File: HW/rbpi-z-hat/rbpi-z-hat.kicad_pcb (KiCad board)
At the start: 4 copper layers, 65 x 30 mm, 98 parts, among them IC1 BQ24315DSGR, J1 RBPI_CONN, J10 JST_GH, J11 Conn_01x10, J12 Conn_01x06, J13 Conn_01x10, J14 Conn_01x06, J15 Conn_01x06, J16 Conn_01x10, J8 Conn_01x06_MountingPin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

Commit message: Changes in Sch & PCB
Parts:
- removed RN9: 1K5, Resistor_SMD:R_Array_Concave_4x0402
- added R13: 1K5, Resistor_SMD:R_0402_1005Metric, F.Cu at (18.4, 19.7)
- added R14: 1K5, Resistor_SMD:R_0402_1005Metric, F.Cu at (18.4, 20.7)
- added R15: 1K5, Resistor_SMD:R_0402_1005Metric, F.Cu at (25.1, 21.1)
- added R16: 1K5, Resistor_SMD:R_0402_1005Metric, F.Cu at (25.1, 20.0)
- R1: footprint Resistor_SMD:R_0603_1608Metric -> Resistor_SMD:R_0402_1005Metric
- moved C5 17.5 mm to (28.1, 20.4), turned to 180 degrees
- moved R1 15.4 mm to (25.1, 18.9), turned to 0 degrees
- moved FB3 15.3 mm to (30.9, 19.4)
- moved U4 14.8 mm to (21.8, 20.1), turned to 0 degrees
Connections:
- net /BARO/BARO_MS_nCS renamed /MS_nCS

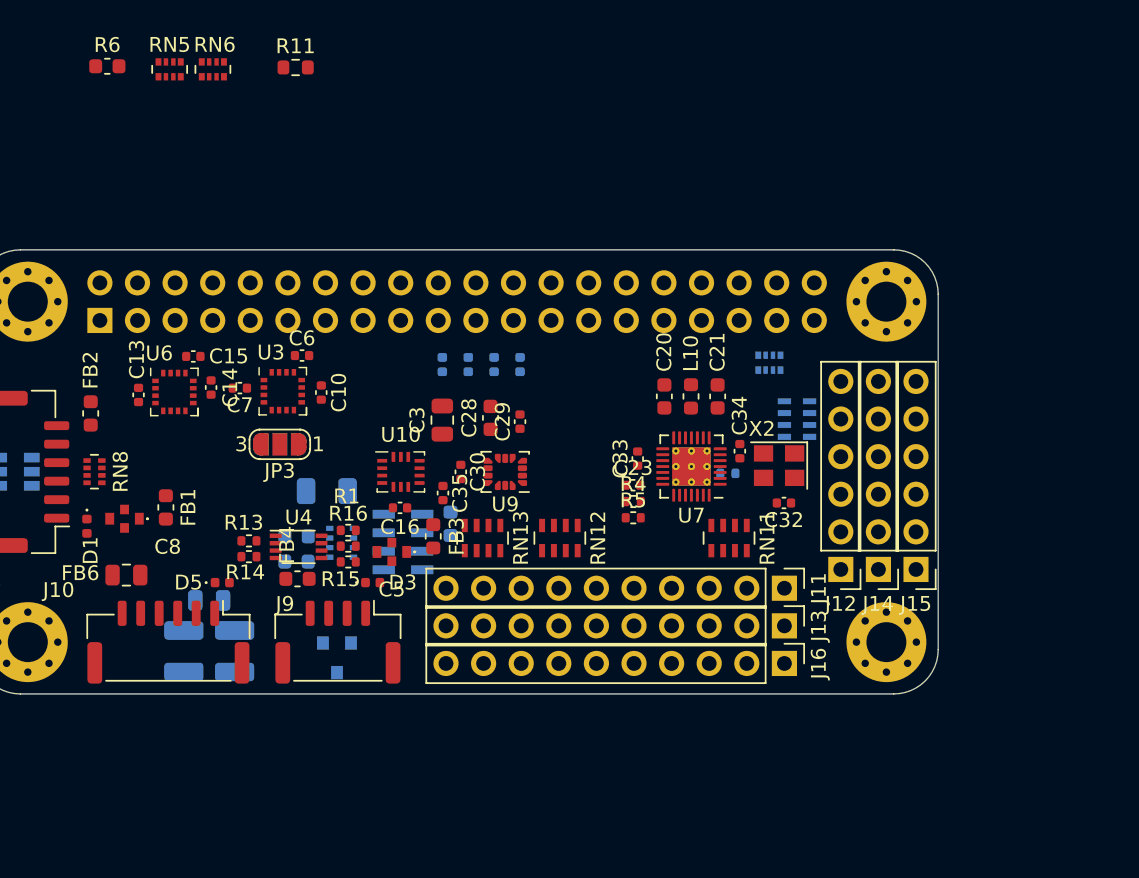
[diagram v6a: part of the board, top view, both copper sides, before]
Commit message: Changed some footprints
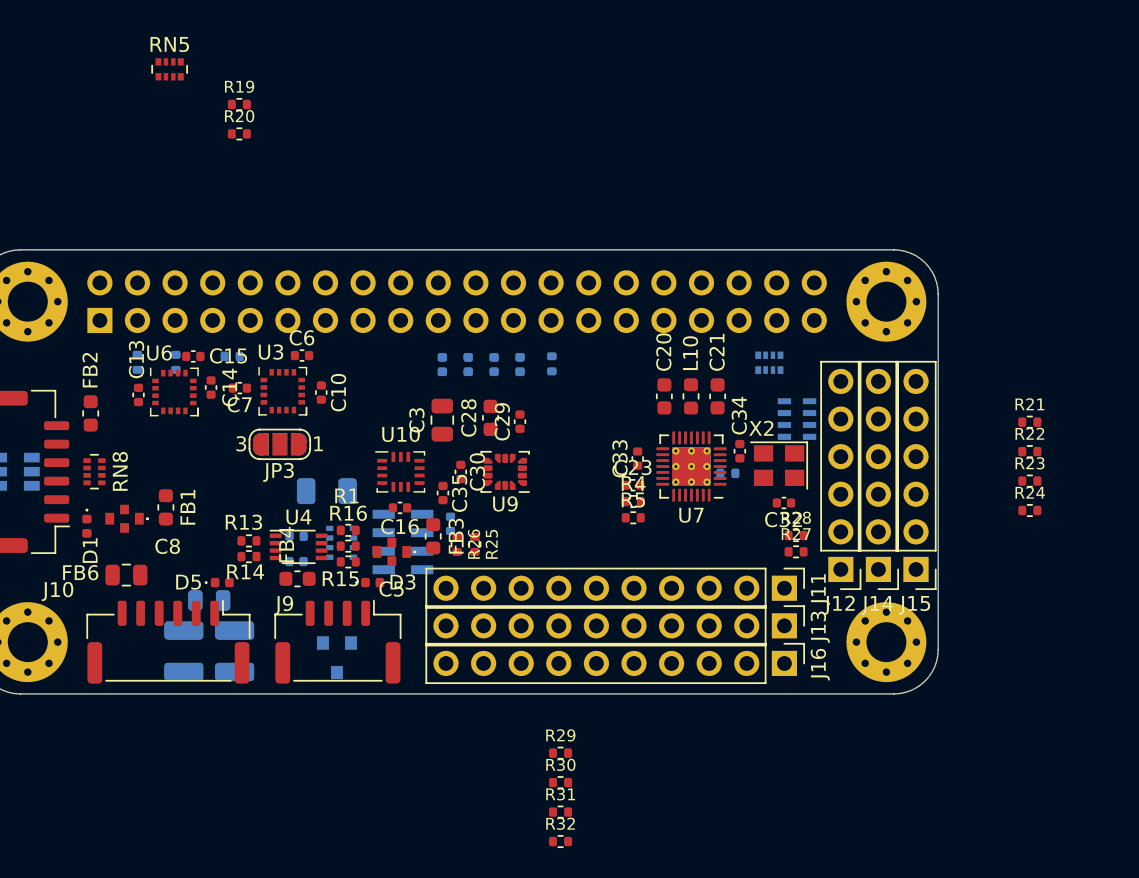
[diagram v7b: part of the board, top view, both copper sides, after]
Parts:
- removed RN11, RN12, RN13: 220R, Resistor_SMD:R_Array_Concave_4x0603
- removed RN6: 10K/4x0402, Resistor_SMD:R_Array_Convex_4x0402
- added R17: 10K, Resistor_SMD:R_0402_1005Metric, B.Cu at (10.9, 7.60)
- added R18: 10K, Resistor_SMD:R_0402_1005Metric, B.Cu at (13.5, 7.60)
- added R19: 10K, Resistor_SMD:R_0402_1005Metric, F.Cu at (17.8, -9.82)
- added R20: 10K, Resistor_SMD:R_0402_1005Metric, F.Cu at (17.8, -7.83)
- added R21: 220К, Resistor_SMD:R_0402_1005Metric, F.Cu at (71.2, 11.6)
- added R22: 220К, Resistor_SMD:R_0402_1005Metric, F.Cu at (71.2, 13.6)
- added R23: 220К, Resistor_SMD:R_0402_1005Metric, F.Cu at (71.2, 15.6)
- added R24: 220К, Resistor_SMD:R_0402_1005Metric, F.Cu at (71.2, 17.6)
- added R25: 220К, Resistor_SMD:R_0402_1005Metric, F.Cu at (33.7, 19.9)
- added R26: 220К, Resistor_SMD:R_0402_1005Metric, F.Cu at (32.5, 19.9)
- added R27: 220К, Resistor_SMD:R_0402_1005Metric, F.Cu at (55.4, 20.4)
- added R28: 220К, Resistor_SMD:R_0402_1005Metric, F.Cu at (55.4, 19.3)
- added R29: 220К, Resistor_SMD:R_0402_1005Metric, F.Cu at (39.5, 34.0)
- added R30: 220К, Resistor_SMD:R_0402_1005Metric, F.Cu at (39.5, 36.0)
- added R31: 220К, Resistor_SMD:R_0402_1005Metric, F.Cu at (39.5, 38.0)
- added R32: 220К, Resistor_SMD:R_0402_1005Metric, F.Cu at (39.5, 40.0)
- C2, C4, C9: footprint Capacitor_SMD:C_0603_1608Metric -> Capacitor_SMD:C_0402_1005Metric
- R11, R6: footprint Resistor_SMD:R_0603_1608Metric -> Resistor_SMD:R_0402_1005Metric; moved to B.Cu
- moved R11 26.5 mm to (38.9, 7.70), turned to 90 degrees
- moved R6 21.3 mm to (17.3, 7.20)

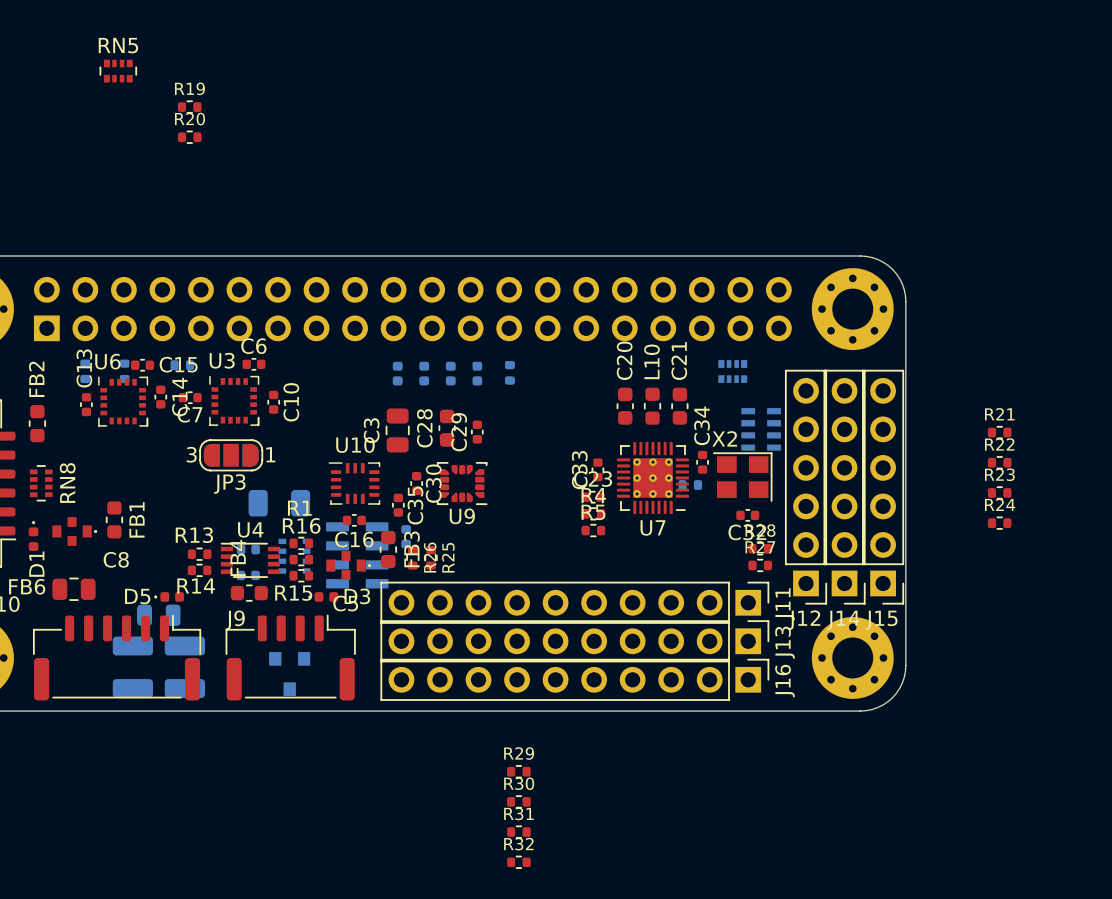
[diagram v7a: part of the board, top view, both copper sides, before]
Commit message: Changed some footprints
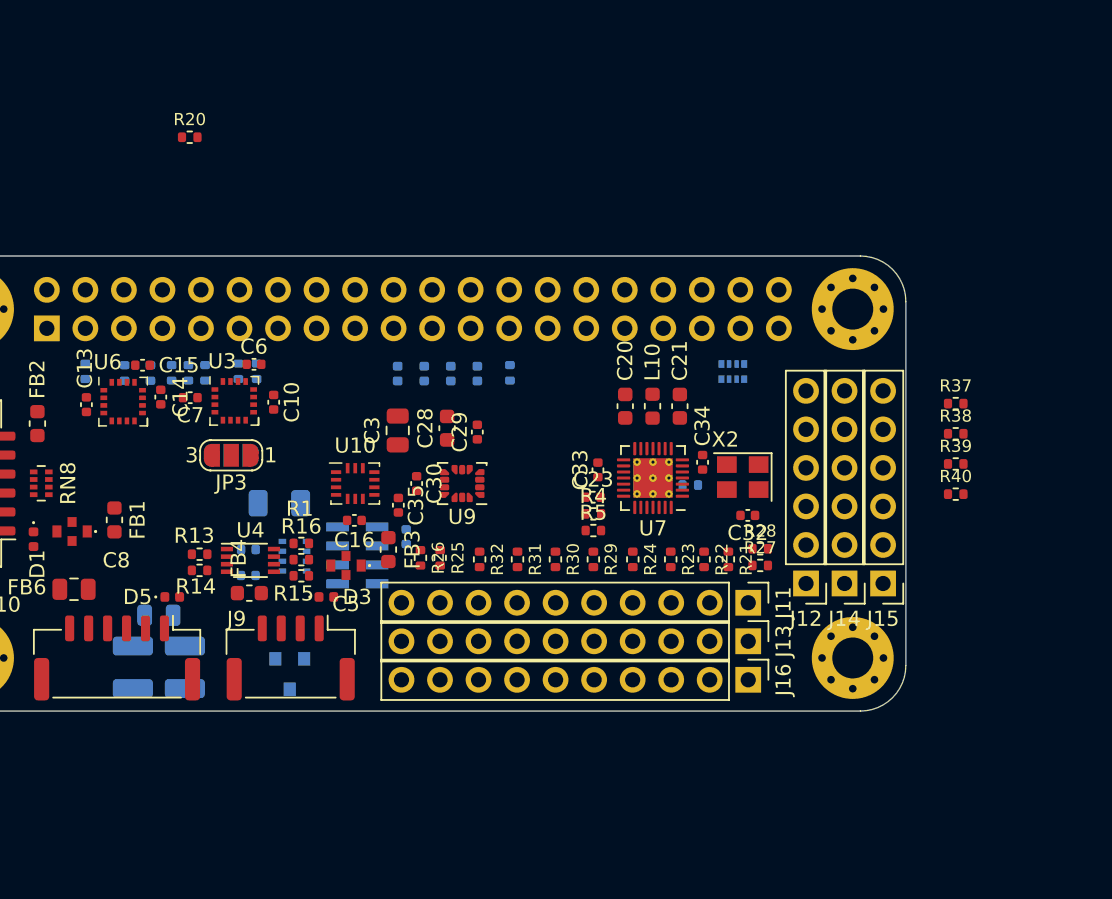
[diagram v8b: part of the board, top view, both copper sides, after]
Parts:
- removed RN14: 220R, Resistor_SMD:R_Array_Concave_4x0603
- removed RN5: 10K/4x0402, Resistor_SMD:R_Array_Convex_4x0402
- added R33: 10K, Resistor_SMD:R_0402_1005Metric, B.Cu at (18.8, 7.70)
- added R34: 10K, Resistor_SMD:R_0402_1005Metric, B.Cu at (15.2, 7.71)
- added R35: 10K, Resistor_SMD:R_0402_1005Metric, B.Cu at (22.2, 7.60)
- added R36: 10K, Resistor_SMD:R_0402_1005Metric, B.Cu at (21.0, 7.60)
- added R37: 220К, Resistor_SMD:R_0402_1005Metric, F.Cu at (68.3, 9.73)
- added R38: 220К, Resistor_SMD:R_0402_1005Metric, F.Cu at (68.3, 11.7)
- added R39: 220К, Resistor_SMD:R_0402_1005Metric, F.Cu at (68.3, 13.7)
- added R40: 220К, Resistor_SMD:R_0402_1005Metric, F.Cu at (68.3, 15.7)
- R19: moved to B.Cu
- moved R24 24.3 mm to (47.0, 20.0), turned to -90 degrees
- moved R23 22.1 mm to (49.5, 20.0), turned to -90 degrees
- moved R22 20.5 mm to (51.7, 20.0), turned to -90 degrees
- moved R32 20.1 mm to (36.9, 20.0), turned to -90 degrees
- moved R21 19.7 mm to (53.3, 20.0), turned to -90 degrees
- moved R31 18.0 mm to (39.4, 20.0), turned to -90 degrees
- moved R19 17.5 mm to (17.7, 7.70), turned to 90 degrees
- moved R30 16.2 mm to (41.9, 20.0), turned to -90 degrees
- moved R29 14.8 mm to (44.4, 20.0), turned to -90 degrees
- moved R6 0.86 mm to (16.6, 7.70), turned to -90 degrees
- moved R25 0.60 mm to (34.3, 19.9)
- moved R26 0.50 mm to (33.0, 19.9)
- moved R18 0.11 mm to (13.5, 7.71)
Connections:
- J1 pad 11: /rbpi/Pin_11_UART_RTS -> /UART_RTS
- J1 pad 12: /rbpi/Pin_12_UART_CTS -> /UART_CTS
